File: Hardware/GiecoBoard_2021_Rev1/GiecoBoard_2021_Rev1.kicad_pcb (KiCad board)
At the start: 2 copper layers, 60 parts, among them J1 Conn_02x02_Top_Bottom, J10 Test_Point, J11 Conn_02x02_Top_Bottom, J2 Conn_02x02_Top_Bottom, J3 Conn_02x02_Top_Bottom, J4 Conn_02x02_Top_Bottom, J5 Conn_02x02_Top_Bottom, J6 Conn_02x02_Top_Bottom, J7 Conn_02x02_Top_Bottom, J8 Conn_02x02_Top_Bottom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

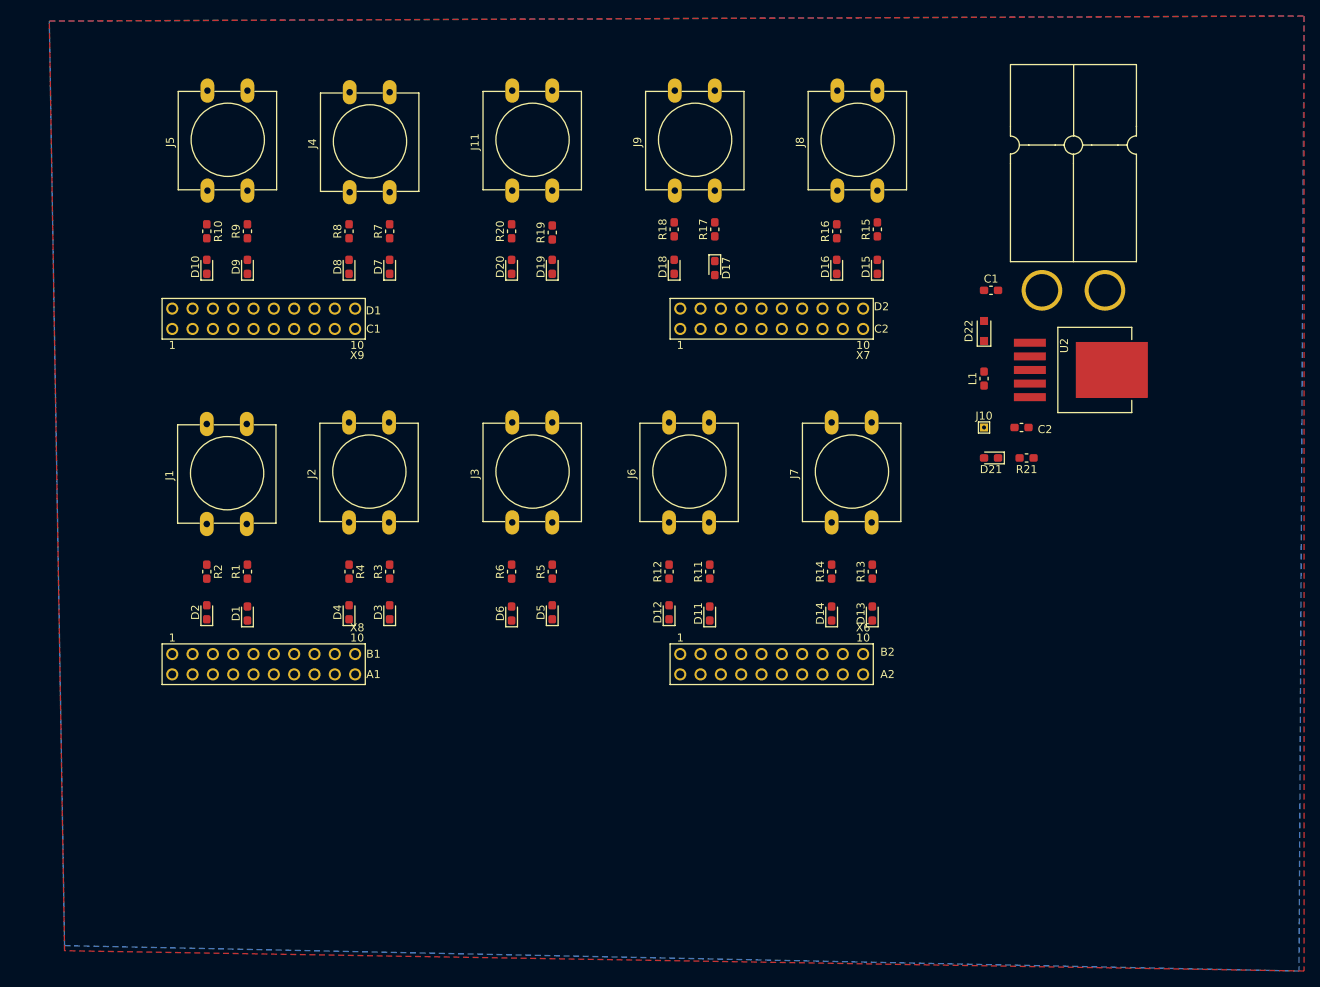
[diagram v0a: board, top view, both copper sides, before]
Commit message: fliped tiva_pin on layout
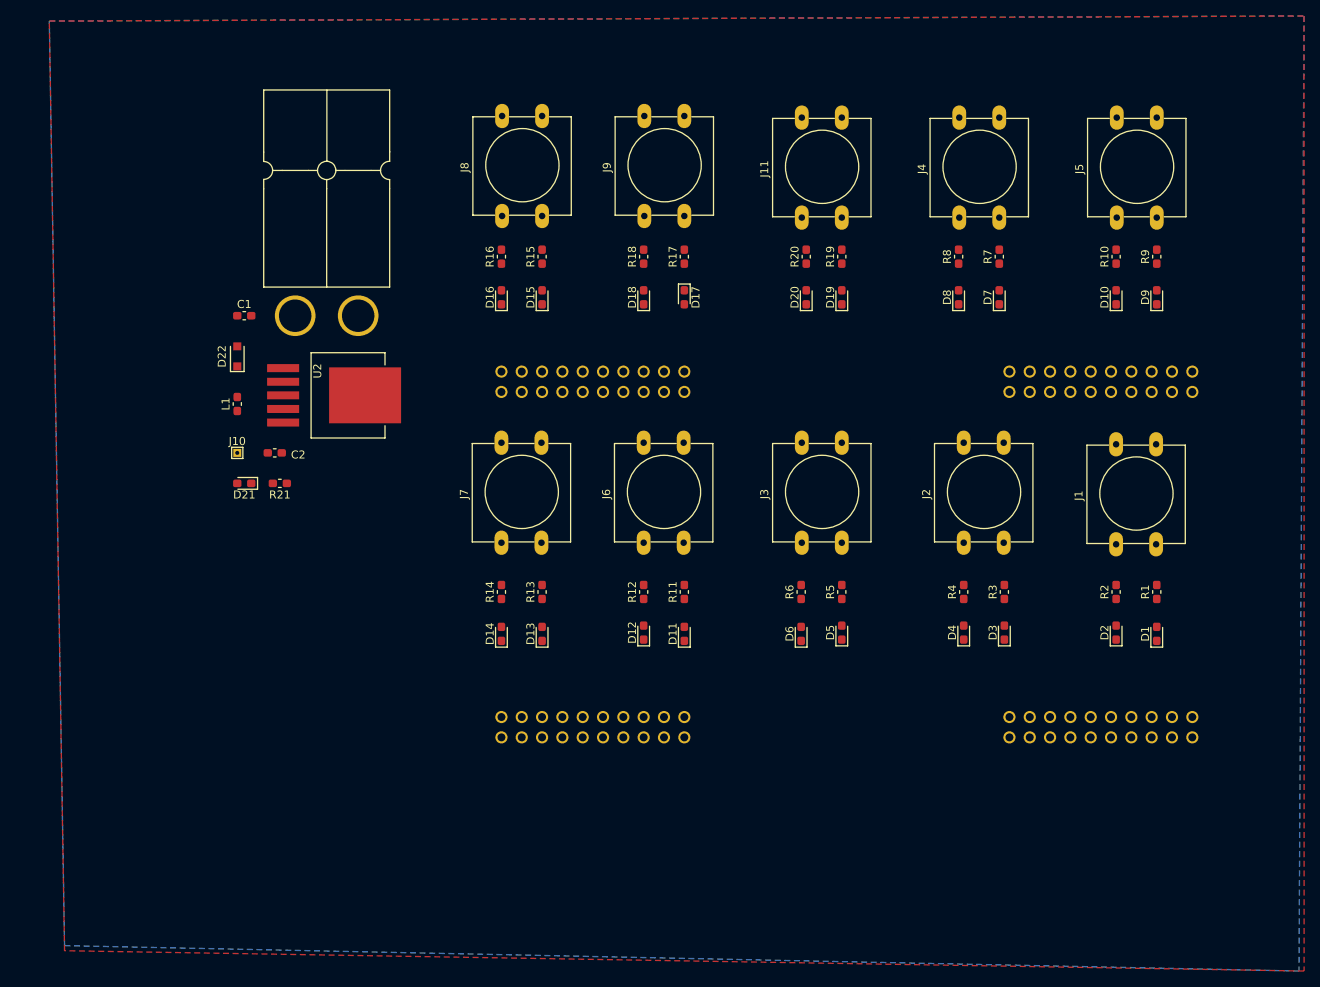
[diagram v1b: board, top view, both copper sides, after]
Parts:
- U1: moved to B.Cu
- moved U1 130.3 mm to (223.5, 137.2), turned to 180 degrees
- moved D9 113.7 mm to (217.8, 80.9)
- moved D10 113.7 mm to (212.7, 80.9)
- moved J5 113.7 mm to (212.8, 70.9)
- moved R9 113.7 mm to (217.8, 75.8)
- moved R10 113.7 mm to (212.7, 75.8), turned to 90 degrees
- moved D1 113.7 mm to (217.8, 123.0)
- moved R1 113.7 mm to (217.8, 117.7)
- moved D2 113.7 mm to (212.7, 122.8)
- moved J1 113.7 mm to (212.7, 111.8)
- moved R2 113.7 mm to (212.7, 117.7), turned to 90 degrees
- moved C1 93.4 mm to (103.7, 83.2)
- moved C2 93.4 mm to (107.6, 100.3)
- moved Conn1 93.4 mm to (118.0, 83.2)
- moved D21 93.4 mm to (103.7, 104.1)
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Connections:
- U1 pad PA4: Send_12VDistribution -> REC_LED_12VDistribution
- U1 pad PA7: Send_PackVoltageDistribution -> REC_LED_PackVoltageDistribution
- U1 pad PB5: REC_LED_NavigationalControl -> Send_NavigationalControl
- U1 pad PD7: Send_ScienceSensor -> REC_LED_ScienceSensor
- U1 pad PE0: REC_LED_ArmArticulation -> Send_ArmArticulation
- U1 pad PE1: Send_ArmArticulation -> REC_LED_ArmArticulation
- U1 pad PE3: REC_LED_ScienceSensor -> Send_ScienceSensor
- U1 pad PK0: Send_NavigationalControl -> REC_LED_NavigationalControl
- U1 pad PK3: REC_LED_12VDistribution -> Send_12VDistribution
- U1 pad PP3: REC_LED_BatteryManagement -> Send_BatteryManagement
- U1 pad PP5: REC_LED_PackVoltageDistribution -> Send_PackVoltageDistribution
- U1 pad PQ1: Send_BatteryManagement -> REC_LED_BatteryManagement

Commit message: wiring on layout
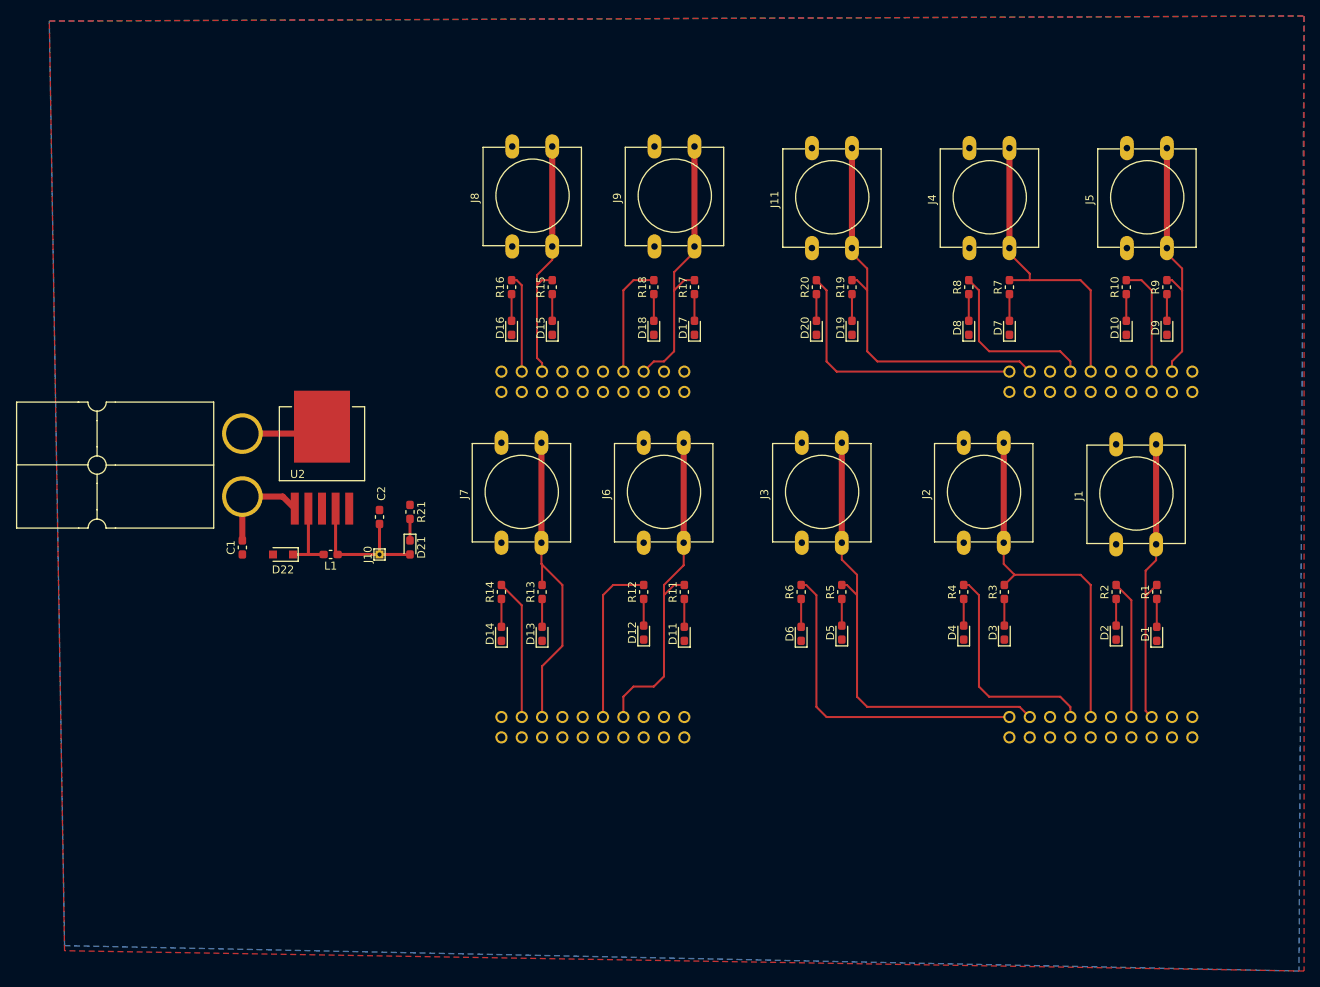
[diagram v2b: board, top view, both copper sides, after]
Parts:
- moved C1 29.0 mm to (103.5, 112.2), turned to 90 degrees
- moved D22 25.4 mm to (108.6, 113.0), turned to 180 degrees
- moved D21 22.2 mm to (124.5, 112.2), turned to 270 degrees
- moved L1 22.1 mm to (114.5, 113.0), turned to 180 degrees
- moved J10 21.8 mm to (120.7, 113.0), turned to 90 degrees
- moved Conn1 20.7 mm to (103.5, 97.9), turned to 0 degrees
- moved R21 16.7 mm to (124.5, 107.7), turned to 270 degrees
- moved C2 15.4 mm to (120.7, 108.3), turned to 90 degrees
- moved U2 7.96 mm to (113.5, 101.0), turned to 0 degrees
- moved J11 4.02 mm to (174.7, 74.7)
- moved J8 4.02 mm to (137.2, 74.5)
- moved J9 4.02 mm to (155.0, 74.5)
- moved J4 4.02 mm to (194.4, 74.7)
- moved J5 4.02 mm to (214.1, 74.7)
- moved D10 4.02 mm to (214.0, 84.7)
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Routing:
- net Send_ScienceActuation: track 0.00 -> 57.6 mm
- net Send_Multimedia: track 0.00 -> 50.0 mm
- net Send_ScienceSensor: track 0.00 -> 45.4 mm
- net Send_NavigationalControl: track 0.00 -> 42.0 mm
- net REC_LED_ScienceActuation: track 0.00 -> 41.1 mm
- net Send_12VDistribution: track 0.00 -> 39.0 mm
- net Send_Gimbal: track 0.00 -> 38.4 mm
- net Send_ArmArticulation: track 0.00 -> 36.9 mm
- net Send_PackVoltageDistribution: track 0.00 -> 34.6 mm
- net REC_LED_Multimedia: track 0.00 -> 34.1 mm
- net Send_DriveCommand: track 0.00 -> 31.7 mm
- net Send_BatteryManagement: track 0.00 -> 31.4 mm
- net REC_LED_ScienceSensor: track 0.00 -> 27.6 mm
- net REC_LED_Gimbal: track 0.00 -> 21.9 mm
- net REC_LED_NavigationalControl: track 0.00 -> 20.8 mm
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
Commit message: add edge cuts,silk screen
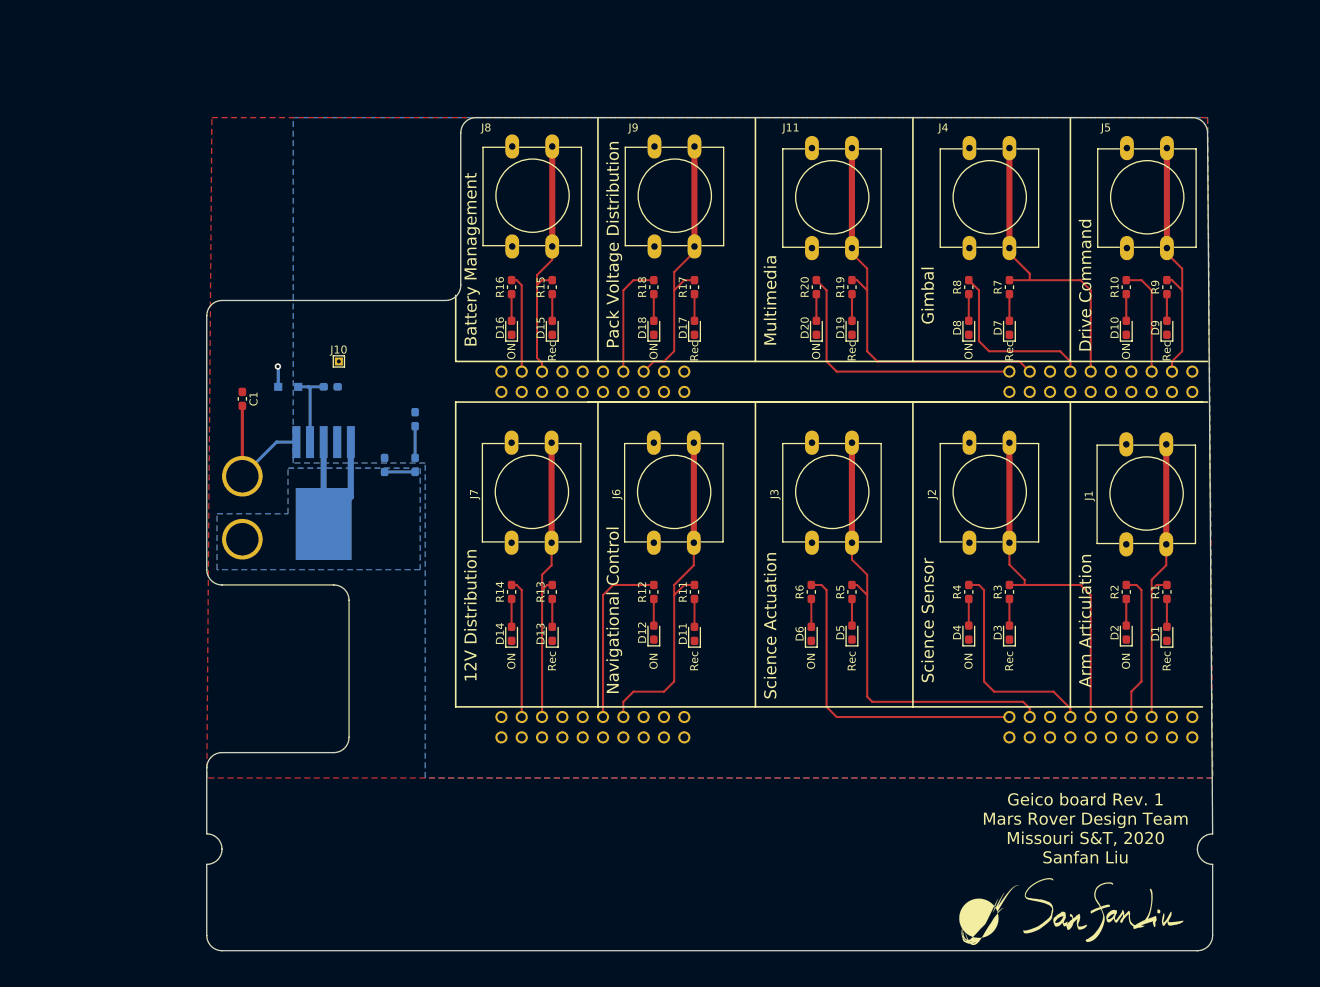
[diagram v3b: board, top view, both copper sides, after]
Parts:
- added G***: LOGO, MRDT_Silkscreens:z_sig_SanfanLiu_sig21.8mmx12.3mm1, F.Cu at (210.8, 157.5)
- added G***: LOGO, MRDT_Silkscreens:0_MRDT_Logo_7.5mm, F.Cu at (196.8, 158.1)
- C2, Conn1, D21, D22, L1, R21, U2: moved to B.Cu
- moved J10 24.7 mm to (115.6, 88.9), turned to 0 degrees
- moved D22 21.0 mm to (109.2, 92.1)
- moved L1 21.0 mm to (114.5, 92.1)
- moved C1 18.6 mm to (103.5, 93.6), turned to 270 degrees
- moved D21 16.0 mm to (125.1, 96.1), turned to 90 degrees
- moved Conn1 13.2 mm to (103.5, 111.1)
- moved C2 6.54 mm to (121.3, 101.8), turned to 270 degrees
- moved R21 5.90 mm to (125.1, 101.8), turned to 90 degrees
- moved U2 4.35 mm to (113.7, 105.3)
- moved D11 1.27 mm to (160.0, 123.0)
- moved D12 1.27 mm to (154.9, 122.8)
- moved D13 1.27 mm to (142.2, 123.0)
- moved D14 1.27 mm to (137.2, 123.0)
- moved D2 1.27 mm to (214.0, 122.8)
- moved D5 1.27 mm to (179.7, 122.8)
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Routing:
- net GND: track 10.3 -> 30.9 mm, vias 0 -> 1
- net +3V3: track 18.7 -> 0.00 mm
- net Net-(C1-Pad2): track 12.7 -> 17.3 mm
- net Send_12VDistribution: track 39.0 -> 36.3 mm
- net Send_NavigationalControl: track 42.0 -> 43.2 mm
- net REC_LED_NavigationalControl: track 20.8 -> 22.1 mm
- net REC_LED_ArmArticulation: track 17.3 -> 18.6 mm
- net Net-(D21-Pad1): track 2.70 -> 3.97 mm
- net Send_ScienceSensor: track 45.4 -> 44.5 mm
- net REC_LED_ScienceActuation: track 41.1 -> 40.2 mm
- net REC_LED_ScienceSensor: track 27.6 -> 26.9 mm
- net Send_ScienceActuation: track 57.6 -> 57.0 mm
- net Net-(D22-Pad1): track 9.57 -> 10.2 mm
- added copper zone on B.Cu, net GND
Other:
- board outline added: 125.7 x 104.1 mm
- board text added: "12V Distribution"
- board text added: "Arm Articulation"
- board text added: "Battery Management"
- board text added: "Drive Command"
- board text added: "Geico board Rev. 1 Mars Rover Design Team Missouri S&T, 2020 Sanfan Liu"
- board text added: "Gimbal"
- board text added: "Multimedia"
- board text added: "Navigational Control"
- board text added: "ON"
- board text added: "Pack Voltage Distribution"
- board text added: "Rec"
- board text added: "Science Actuation"
- board text added: "Science Sensor"

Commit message: Layout review update
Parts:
- Conn1: footprint MRDT_Connectors:Anderson_2_Horizontal_Side_by_Side -> MRDT_Connectors:Anderson_2_Vertical_Sidy_by_Side; moved to F.Cu
- D22: value D_Schottky -> 1n5582; footprint Diode_SMD:D_SOD-323_HandSoldering -> Diode_THT:D_DO-201AD_P15.24mm_Horizontal; moved to F.Cu
- U2: value LM2576D2TR4 -> LM2576SX-3.3
- moved D22 10.5 mm to (118.7, 87.6)
- moved J10 9.53 mm to (125.1, 88.9)
- moved L1 9.52 mm to (124.1, 92.1)
- moved Conn1 0.34 mm to (103.5, 110.8), turned to 90 degrees
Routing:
- net Net-(D22-Pad1): track 10.2 -> 20.1 mm
- net GND: track 30.9 -> 28.4 mm, vias 1 -> 0
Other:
- board text added: "Geico board Rev. 1 Mars Rover Design Team Missouri S&T, 2021 Sanfan Liu"
- board text removed: "Geico board Rev. 1 Mars Rover Design Team Missouri S&T, 2020 Sanfan Liu"

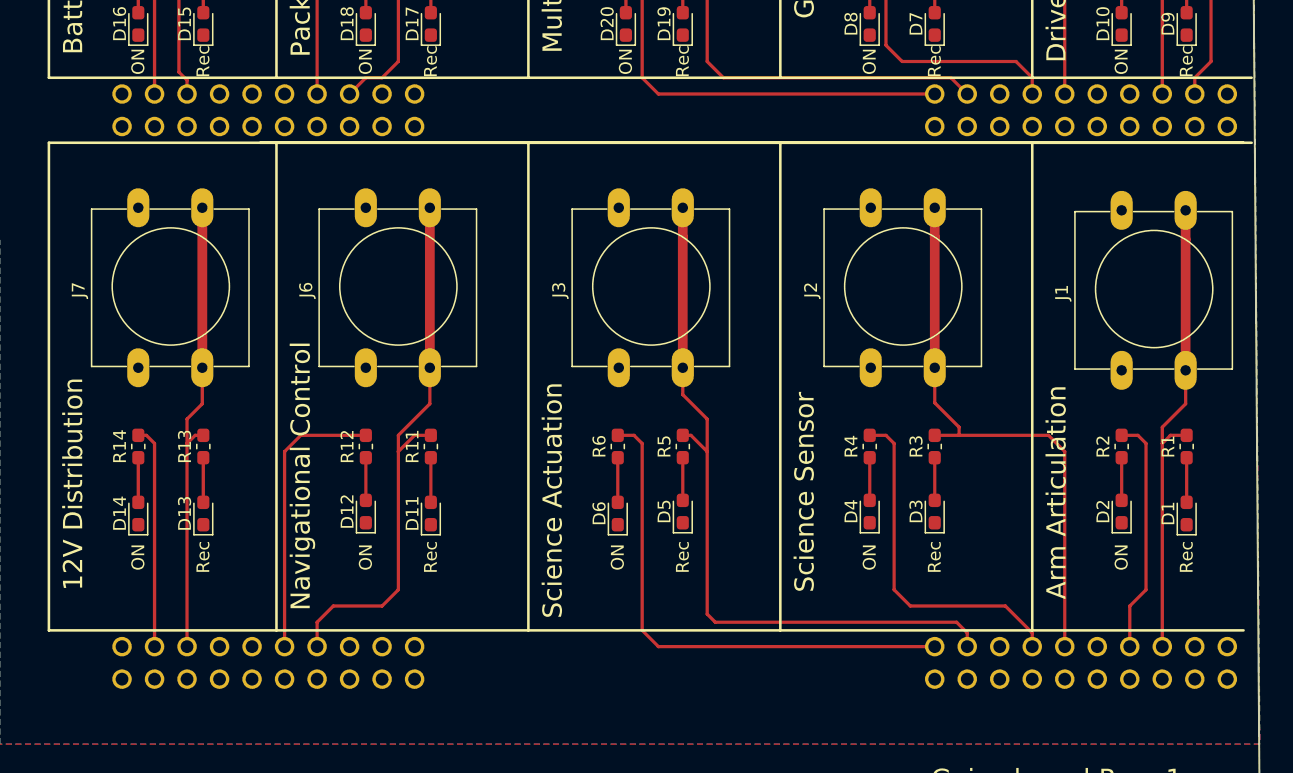
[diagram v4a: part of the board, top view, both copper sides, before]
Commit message: change TIVA footprint
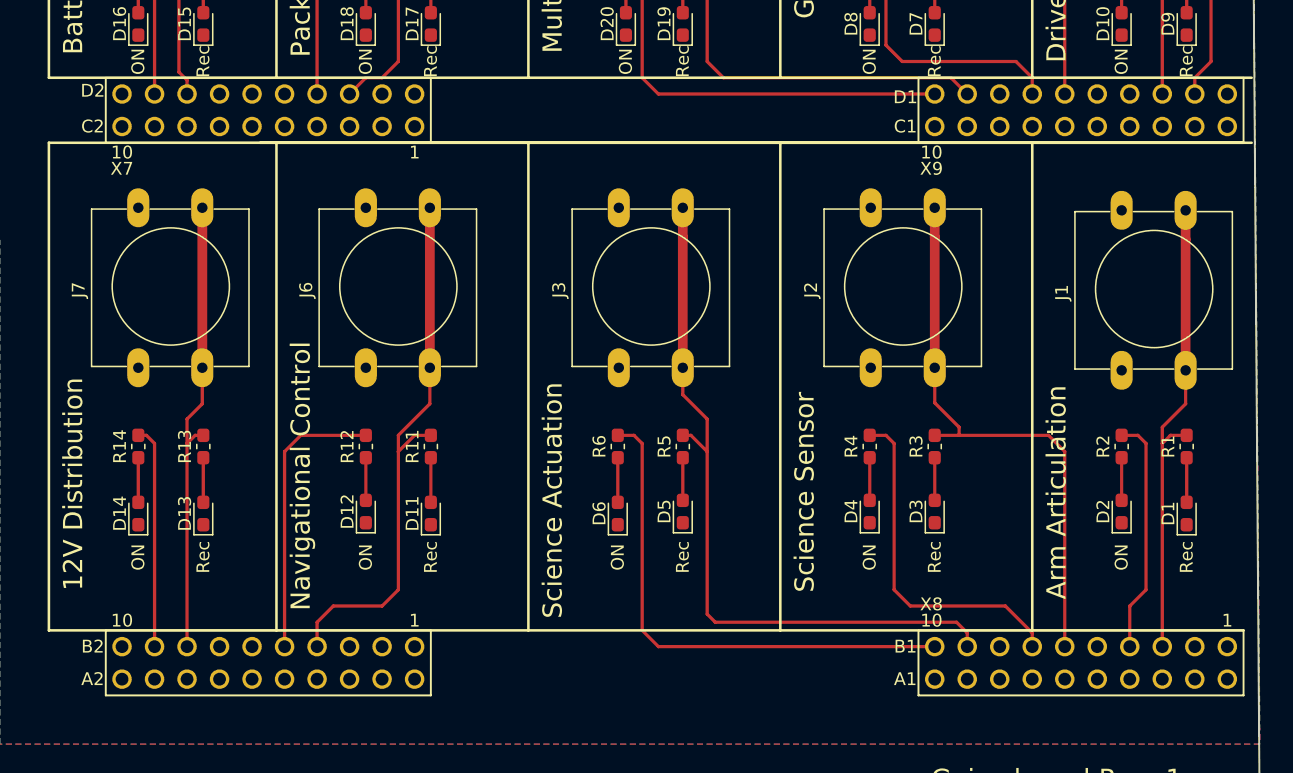
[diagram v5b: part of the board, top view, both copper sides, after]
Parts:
- U1: footprint MRDT_Shields:TM4C129E_Launchpad_FULL_THT_TOP -> MRDT_Shields:TM4C129E_Launchpad_FULL_THT_BOTTOM
